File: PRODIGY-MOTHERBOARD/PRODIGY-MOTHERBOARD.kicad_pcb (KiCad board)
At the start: 2 copper layers, 183 parts, among them J1 USB_A, J10 CAN, J11 SERIAL, J12 MOTOR, J13 MOTOR, J15 Barrel_Jack_MountingPin, J16 AudioJack3, J19 KEYPAD_MATRIX, J2 SERVO, J20 Ultrasonic, J21 GPIO, J22 GPIO, J23 GPIO, J24 12V OUT, J3 SERVO, J4 SERVO, J5 GPIO, J6 DM3BT-DSF-PEJS/C, J7 A_OUT, J8 SPI_OUT, J9 I2C, P1 USB_C_Plug, P2 USB_C_Plug, Q1 Q_Photo_NPN, Q2 NJFET, Q3 BC850, Q4 DMP2045U-7, SW1 SW_SPST, SW2 SW_SPST, SW3 SW_SPST, SW4 SW_SPST, SW5 SW_SPST, U1 PN5321A3HN_C1xx, U10 DRV8870DDA, U11 CR2013-MI2120, U12 PCF8574, U13 SN74LVC1T45DBV, U15 CC56-12YWA, U16 LM386, U17 TXS0108EPW, U18 PCA9306DC, U19 PCF8574, U20 LIS2DH12TR, U21 DRV8870DDA, U22 IP4252CZ16, U23 MCP6021RT-E/OT, U3 TPS22810DRV, U4 TPS54331DR, U5 TPS54331DR, U6 Si4460, U7 LM386, U8 HDC1080, U9 SN65HVD232

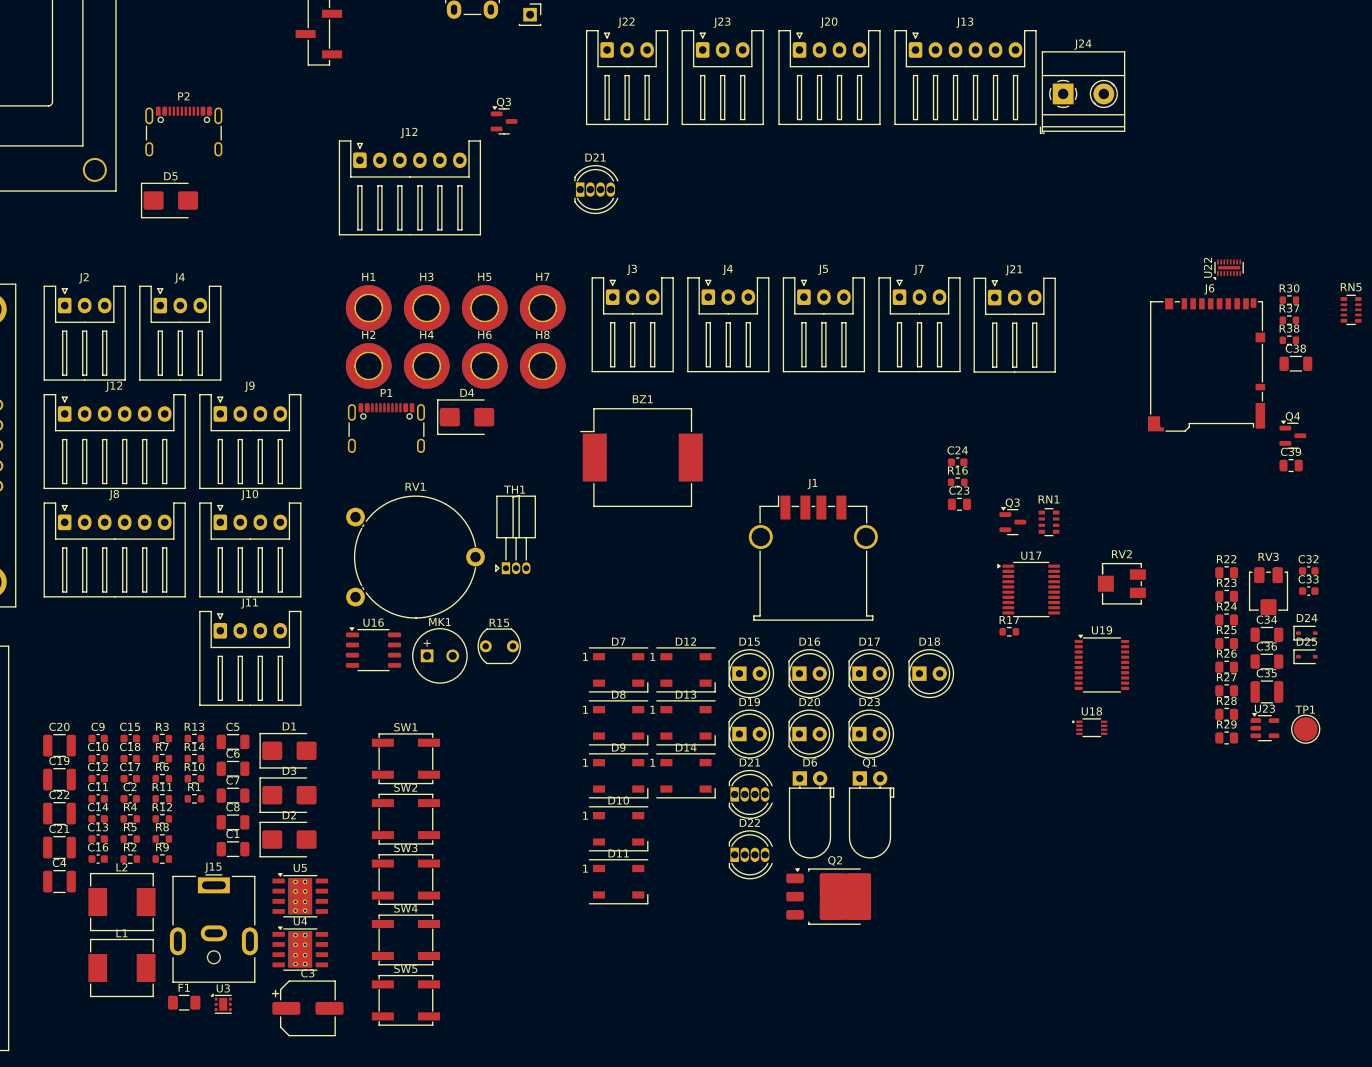
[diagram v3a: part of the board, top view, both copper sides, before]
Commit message: LEDs schematic done.
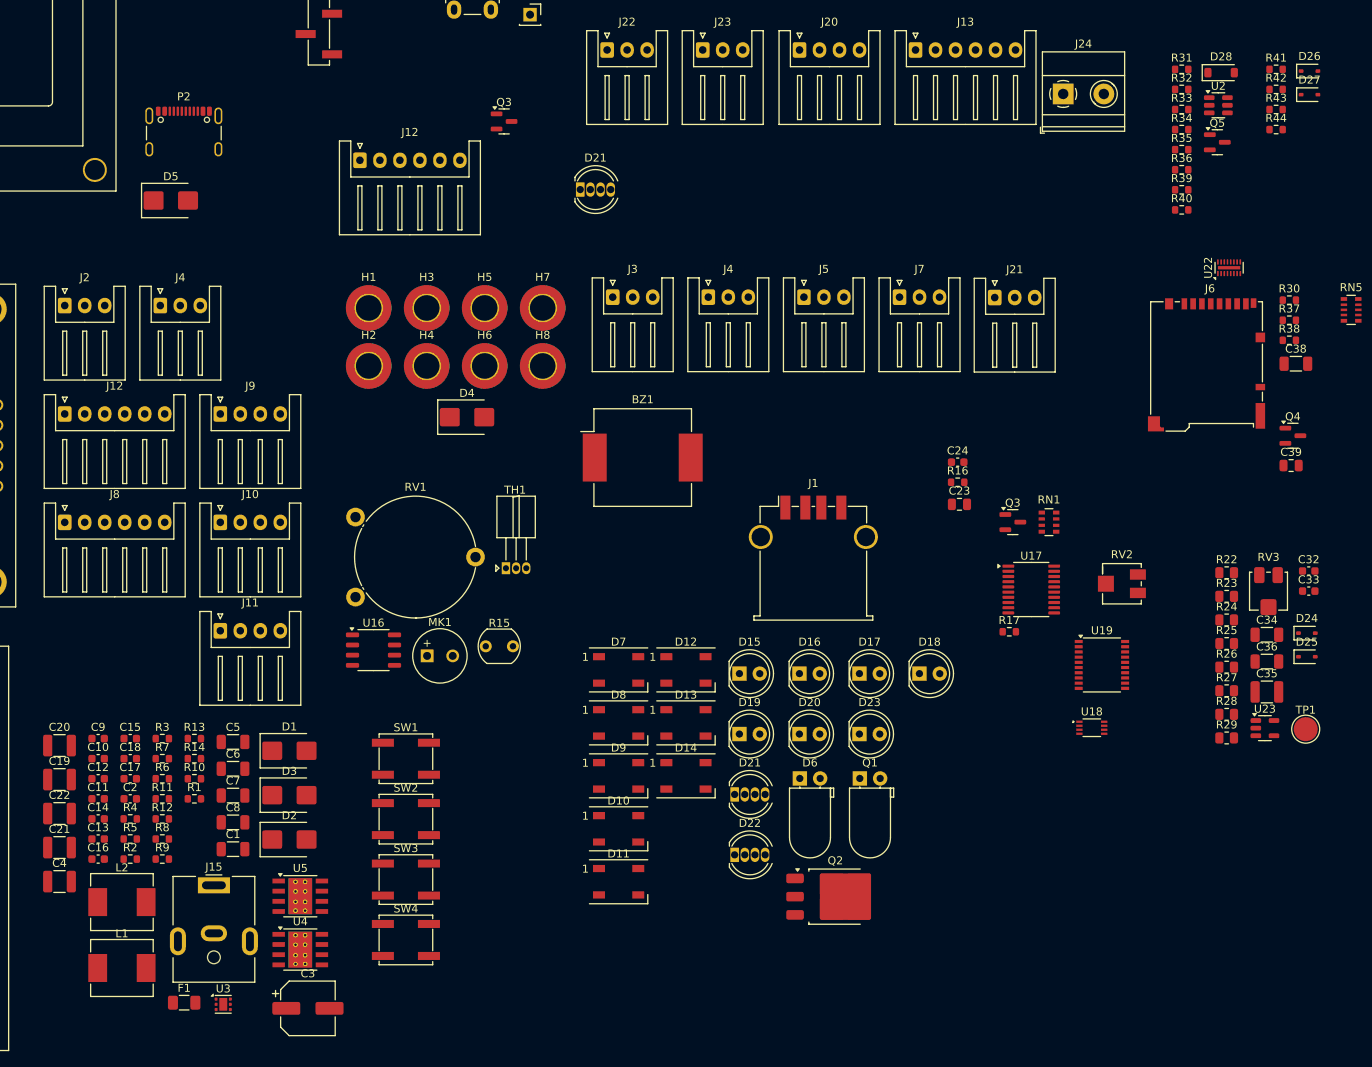
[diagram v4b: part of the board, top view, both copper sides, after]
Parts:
- removed P1: USB_C_Plug, Connector_USB:USB_C_Receptacle_GCT_USB4105-xx-A_16P_TopMnt_Horizontal
- removed SW5: SW_SPST, Button_Switch_SMD:SW_SPST_EVQP0
- added D26: SD05_SOD323, Diode_SMD:D_SOD-323, F.Cu at (244.8, 40.7)
- added D27: SD05_SOD323, Diode_SMD:D_SOD-323, F.Cu at (244.8, 43.6)
- added D28: 1N4148W, Diode_SMD:D_SOD-123, F.Cu at (233.8, 40.9)
- added Q5: BC850, Package_TO_SOT_SMD:SOT-23, F.Cu at (233.3, 49.6)
- added R31: 100, Resistor_SMD:R_0603_1608Metric, F.Cu at (228.9, 40.5)
- added R32: 10k, Resistor_SMD:R_0603_1608Metric, F.Cu at (228.9, 43.0)
- added R33: 10k, Resistor_SMD:R_0603_1608Metric, F.Cu at (228.9, 45.5)
- added R34: 100, Resistor_SMD:R_0603_1608Metric, F.Cu at (228.9, 48.0)
- added R35: 10k, Resistor_SMD:R_0603_1608Metric, F.Cu at (228.9, 50.5)
- added R36: 100, Resistor_SMD:R_0603_1608Metric, F.Cu at (228.9, 53.0)
- added R39: 10k, Resistor_SMD:R_0603_1608Metric, F.Cu at (228.9, 55.5)
- added R40: 100, Resistor_SMD:R_0603_1608Metric, F.Cu at (228.9, 58.0)
- added R41: 10k, Resistor_SMD:R_0603_1608Metric, F.Cu at (240.7, 40.5)
- added R42: 100, Resistor_SMD:R_0603_1608Metric, F.Cu at (240.7, 43.0)
- added R43: 5.1k, Resistor_SMD:R_0603_1608Metric, F.Cu at (240.7, 45.5)
- added R44: 5.1k, Resistor_SMD:R_0603_1608Metric, F.Cu at (240.7, 48.0)
- added U2: SN74LVC1T45DBV, Package_TO_SOT_SMD:SOT-23-6, F.Cu at (233.5, 45.0)
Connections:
- BZ1 pad 1: unconnected-(BZ1---Pad1) -> +3V3
- BZ1 pad 2: unconnected-(BZ1-+-Pad2) -> Net-(BZ1-+)
- D10 pad 1: unconnected-(D10-VDD-Pad1) -> +5V (x2)
- D10 pad 2: unconnected-(D10-DOUT-Pad2) -> Net-(D10-DOUT) (x2)
- D10 pad 3: unconnected-(D10-VSS-Pad3) -> GND (x2)
- D10 pad 4: unconnected-(D10-DIN-Pad4) -> Net-(D10-DIN) (x2)
- D11 pad 1: unconnected-(D11-VDD-Pad1) -> +5V (x2)
- D11 pad 2: unconnected-(D11-DOUT-Pad2) -> Net-(D11-DOUT) (x2)
- D11 pad 3: unconnected-(D11-VSS-Pad3) -> GND (x2)
- D11 pad 4: unconnected-(D11-DIN-Pad4) -> Net-(D10-DOUT) (x2)
- D12 pad 1: unconnected-(D12-VDD-Pad1) -> +5V (x2)
- D12 pad 2: unconnected-(D12-DOUT-Pad2) -> Net-(D12-DOUT) (x2)
- D12 pad 3: unconnected-(D12-VSS-Pad3) -> GND (x2)
- D12 pad 4: unconnected-(D12-DIN-Pad4) -> Net-(D11-DOUT) (x2)
- D13 pad 1: unconnected-(D13-VDD-Pad1) -> +5V (x2)
- D13 pad 2: unconnected-(D13-DOUT-Pad2) -> Net-(D13-DOUT) (x2)
- D13 pad 3: unconnected-(D13-VSS-Pad3) -> GND (x2)
- D13 pad 4: unconnected-(D13-DIN-Pad4) -> Net-(D12-DOUT) (x2)
- D14 pad 1: unconnected-(D14-VDD-Pad1) -> +5V (x2)
- D14 pad 2: unconnected-(D14-DOUT-Pad2) -> /digital/DIGITAL_NEOPIXEL_OUT (x2)
- D14 pad 3: unconnected-(D14-VSS-Pad3) -> GND (x2)
- D14 pad 4: unconnected-(D14-DIN-Pad4) -> Net-(D13-DOUT) (x2)
- D4 pad 1: unconnected-(D4-K-Pad1) -> +5V (x2)
- D4 pad 2: unconnected-(D4-A-Pad2) -> Net-(D4-A) (x2)
- D7 pad 1: unconnected-(D7-VDD-Pad1) -> +5V (x2)
- D7 pad 2: unconnected-(D7-DOUT-Pad2) -> Net-(D7-DOUT) (x2)
- D7 pad 3: unconnected-(D7-VSS-Pad3) -> GND (x2)
- D7 pad 4: unconnected-(D7-DIN-Pad4) -> Net-(D7-DIN) (x2)
- D8 pad 1: unconnected-(D8-VDD-Pad1) -> +5V (x2)
- D8 pad 2: unconnected-(D8-DOUT-Pad2) -> Net-(D8-DOUT) (x2)
- D8 pad 3: unconnected-(D8-VSS-Pad3) -> GND (x2)
- D8 pad 4: unconnected-(D8-DIN-Pad4) -> Net-(D7-DOUT) (x2)
- D9 pad 1: unconnected-(D9-VDD-Pad1) -> +5V (x2)
- D9 pad 2: unconnected-(D9-DOUT-Pad2) -> Net-(D10-DIN) (x2)
- D9 pad 3: unconnected-(D9-VSS-Pad3) -> GND (x2)
- D9 pad 4: unconnected-(D9-DIN-Pad4) -> Net-(D8-DOUT) (x2)
- RN2 pad 5: unconnected-(RN2-R4-Pad5) -> /SPI/CS_BREAKOUT

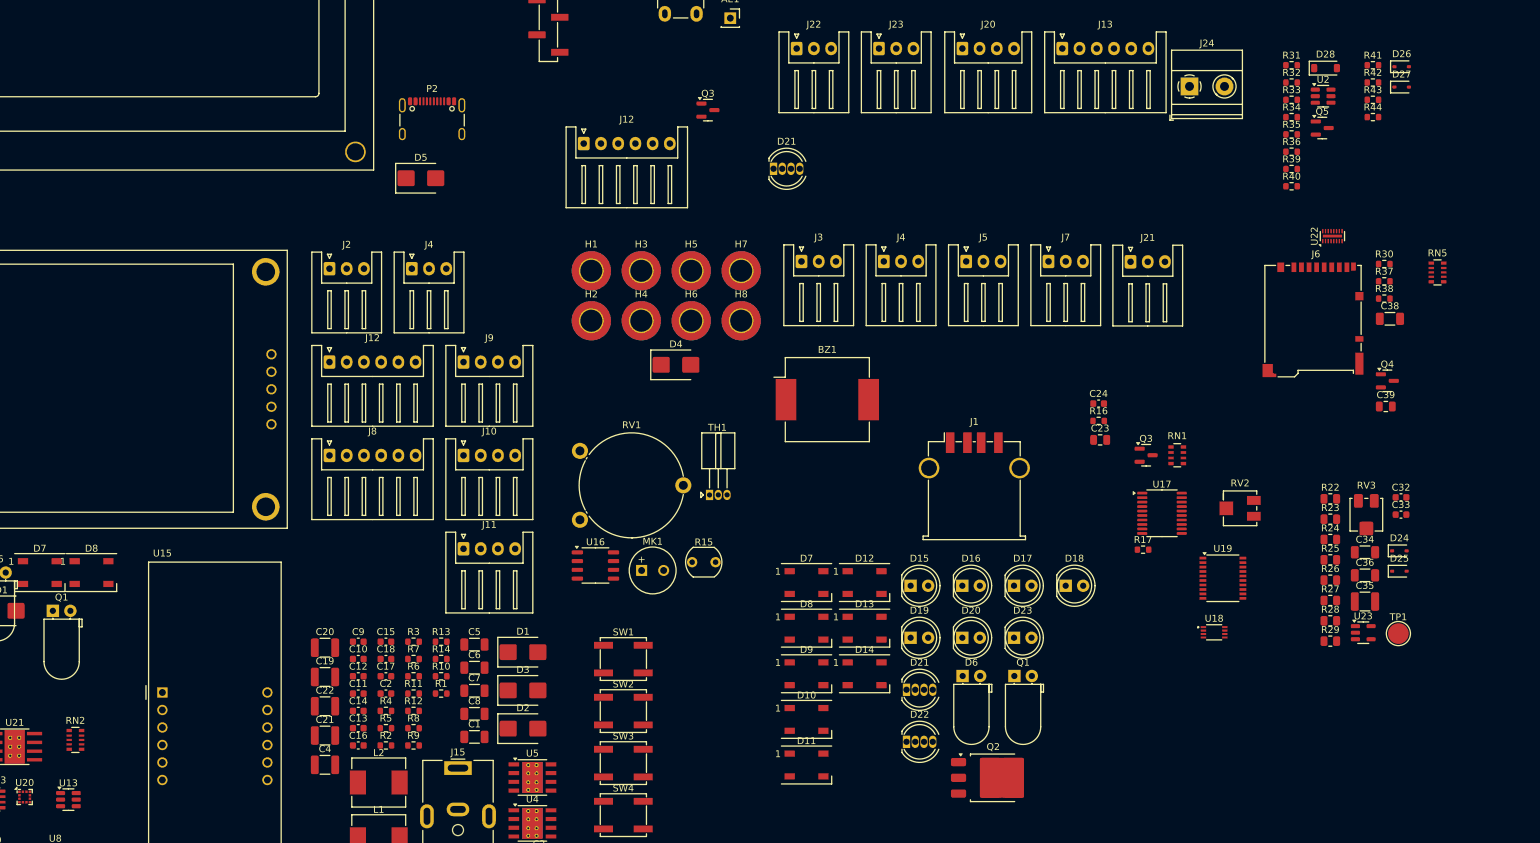
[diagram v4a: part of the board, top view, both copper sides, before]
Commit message: Digital section done.
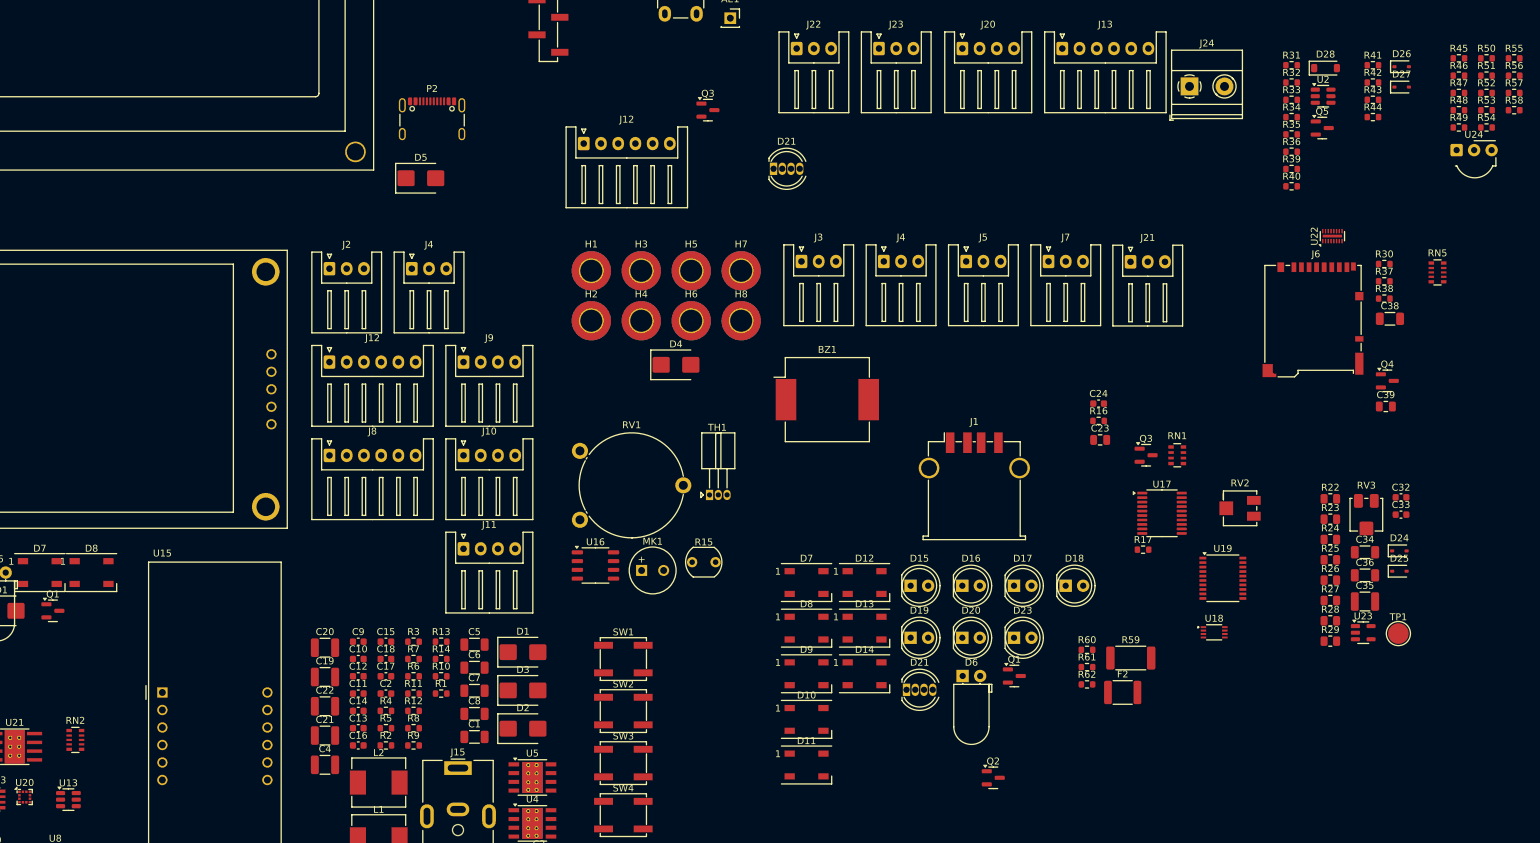
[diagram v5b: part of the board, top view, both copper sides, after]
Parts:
- removed D22: LED_ABGR, LED_THT:LED_D5.0mm-4_RGB
- added F2: 1A PTC, Fuse:Fuse_1812_4532Metric, F.Cu at (204.4, 131.5)
- added R45: 1k, Resistor_SMD:R_0603_1608Metric, F.Cu at (253.2, 39.5)
- added R46: 1k, Resistor_SMD:R_0603_1608Metric, F.Cu at (253.2, 42.0)
- added R47: 1k, Resistor_SMD:R_0603_1608Metric, F.Cu at (253.2, 44.5)
- added R48: 1k, Resistor_SMD:R_0603_1608Metric, F.Cu at (253.2, 47.0)
- added R49: 1k, Resistor_SMD:R_0603_1608Metric, F.Cu at (253.2, 49.5)
- added R50: 1k, Resistor_SMD:R_0603_1608Metric, F.Cu at (257.2, 39.5)
- added R51: 1k, Resistor_SMD:R_0603_1608Metric, F.Cu at (257.2, 42.0)
- added R52: 1k, Resistor_SMD:R_0603_1608Metric, F.Cu at (257.2, 44.5)
- added R53: 1k, Resistor_SMD:R_0603_1608Metric, F.Cu at (257.2, 47.0)
- added R54: 1k, Resistor_SMD:R_0603_1608Metric, F.Cu at (257.2, 49.5)
- added R55: 1k, Resistor_SMD:R_0603_1608Metric, F.Cu at (261.2, 39.5)
- added R56: 1k, Resistor_SMD:R_0603_1608Metric, F.Cu at (261.2, 42.0)
- added R57: 39, Resistor_SMD:R_0603_1608Metric, F.Cu at (261.2, 44.5)
- added R58: 100, Resistor_SMD:R_0603_1608Metric, F.Cu at (261.2, 47.0)
- added R59: DNP, Resistor_SMD:R_2512_6332Metric, F.Cu at (205.5, 126.5)
- added R60: 10k, Resistor_SMD:R_0603_1608Metric, F.Cu at (199.2, 125.3)
- added R61: 100, Resistor_SMD:R_0603_1608Metric, F.Cu at (199.2, 127.8)
- added R62: 10k, Resistor_SMD:R_0603_1608Metric, F.Cu at (199.2, 130.3)
- added U24: TSDP341xx, OptoDevice:Vishay_MOLD-3Pin, F.Cu at (252.8, 52.8)
- Q1 (x2): value Q_Photo_NPN -> BC850; footprint LED_THT:LED_D5.0mm_Horizontal_O1.27mm_Z3.0mm_IRBlack -> Package_TO_SOT_SMD:SOT-23
- Q2: value NJFET -> BS870; footprint Package_TO_SOT_SMD:TO-252-3_TabPin2 -> Package_TO_SOT_SMD:SOT-23
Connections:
- net /POWER/VIN renamed +12V
- D15 pad 1: unconnected-(D15-K-Pad1) -> Net-(D15-K) (x2)
- D15 pad 2: unconnected-(D15-A-Pad2) -> /digital/DIGITAL_LED_12V (x2)
- D16 pad 1: unconnected-(D16-K-Pad1) -> Net-(D16-K) (x2)
- D16 pad 2: unconnected-(D16-A-Pad2) -> /digital/DIGITAL_LED_5V (x2)
- D17 pad 1: unconnected-(D17-K-Pad1) -> Net-(D17-K) (x2)
- D17 pad 2: unconnected-(D17-A-Pad2) -> /digital/DIGITAL_LED_3V3 (x2)
- D18 pad 1: unconnected-(D18-K-Pad1) -> Net-(D18-K)
- D18 pad 2: unconnected-(D18-A-Pad2) -> /digital/DIGITAL_LED_0
- D19 pad 1: unconnected-(D19-K-Pad1) -> Net-(D19-K)
- D19 pad 2: unconnected-(D19-A-Pad2) -> /digital/DIGITAL_LED_1
- D20 pad 1: unconnected-(D20-K-Pad1) -> Net-(D20-K)
- D20 pad 2: unconnected-(D20-A-Pad2) -> /digital/DIGITAL_LED_2
- D23 pad 1: unconnected-(D23-K-Pad1) -> Net-(D23-K)
- D23 pad 2: unconnected-(D23-A-Pad2) -> Net-(D23-A)
- D6 pad 1: unconnected-(D6-K-Pad1) -> Net-(D6-K) (x2)
- D6 pad 2: unconnected-(D6-A-Pad2) -> Net-(D6-A) (x2)
- Q1 pad 1: unconnected-(Q1-C-Pad1) -> Net-(Q1-B) (x2)
- Q1 pad 2: unconnected-(Q1-E-Pad2) -> GND (x2)
- Q2 pad 1: unconnected-(Q2-D-Pad1) -> Net-(Q2-G)
- Q2 pad 2: unconnected-(Q2-G-Pad2) -> GND
- Q2 pad 3: unconnected-(Q2-S-Pad3) -> Net-(D23-K)
